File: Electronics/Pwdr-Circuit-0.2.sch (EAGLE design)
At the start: 23 parts, among them U1 LM317T, U2 ARDUINO-MEGASHIELD, U5 ULN2003, U6 ULN2003

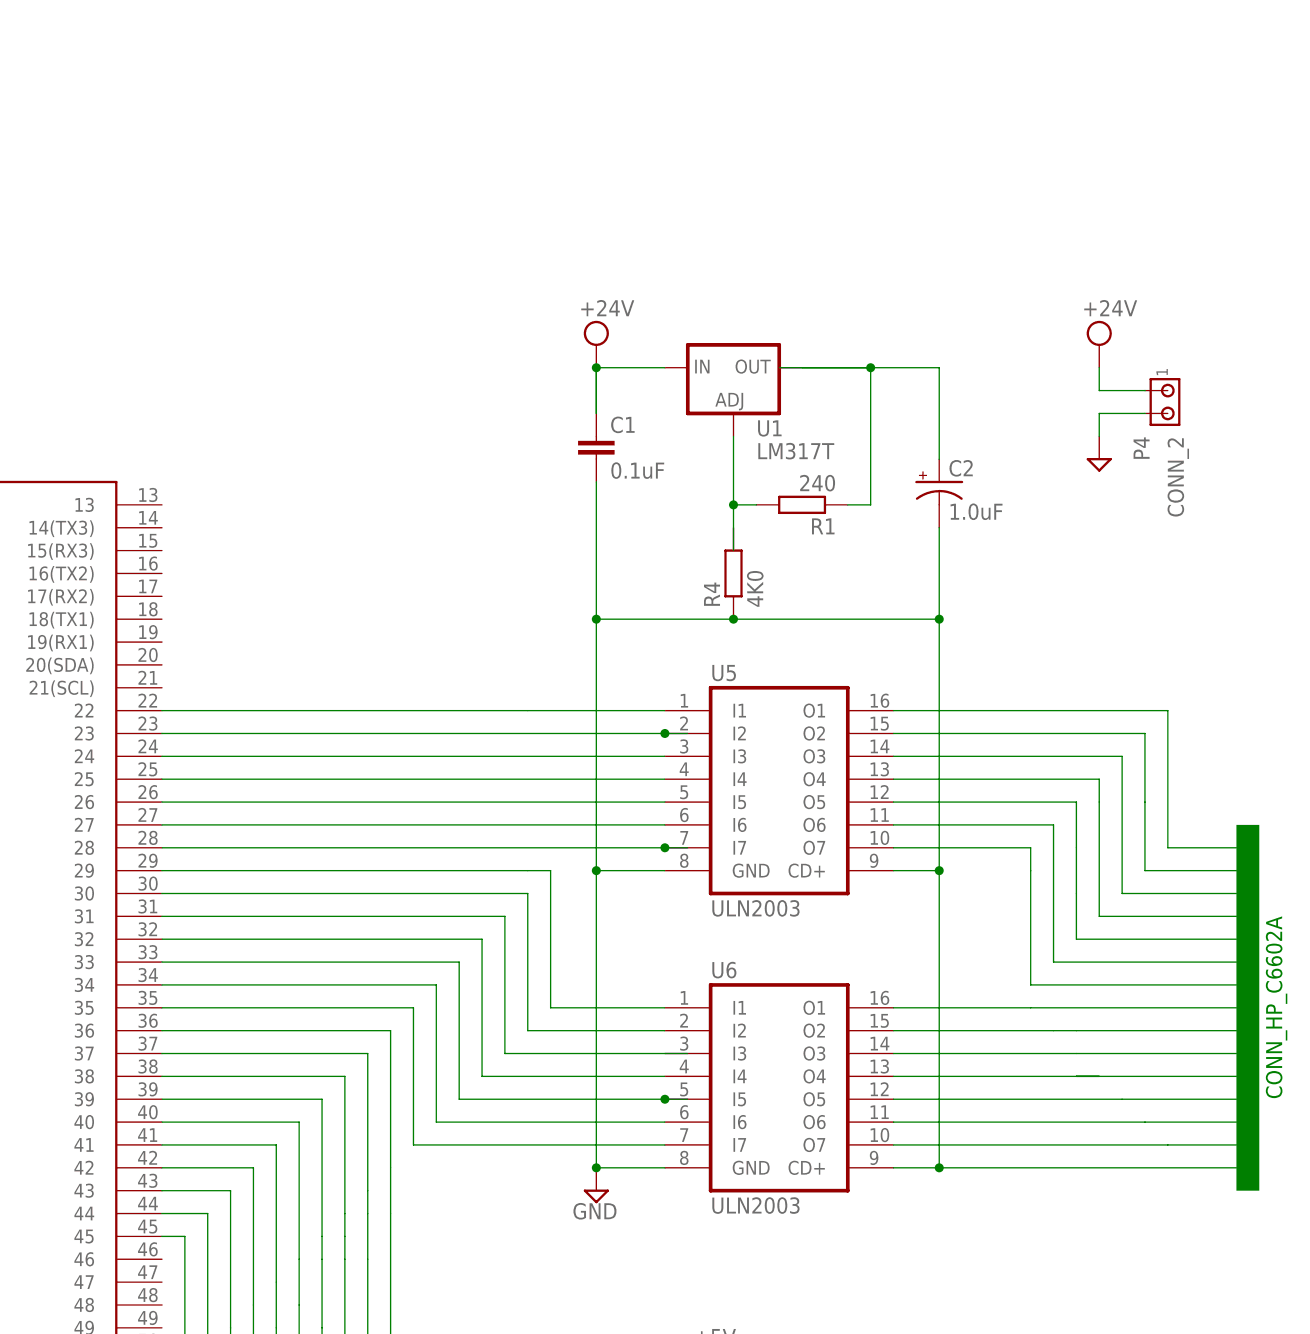
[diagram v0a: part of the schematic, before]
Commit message: Added shutdown to schematic.
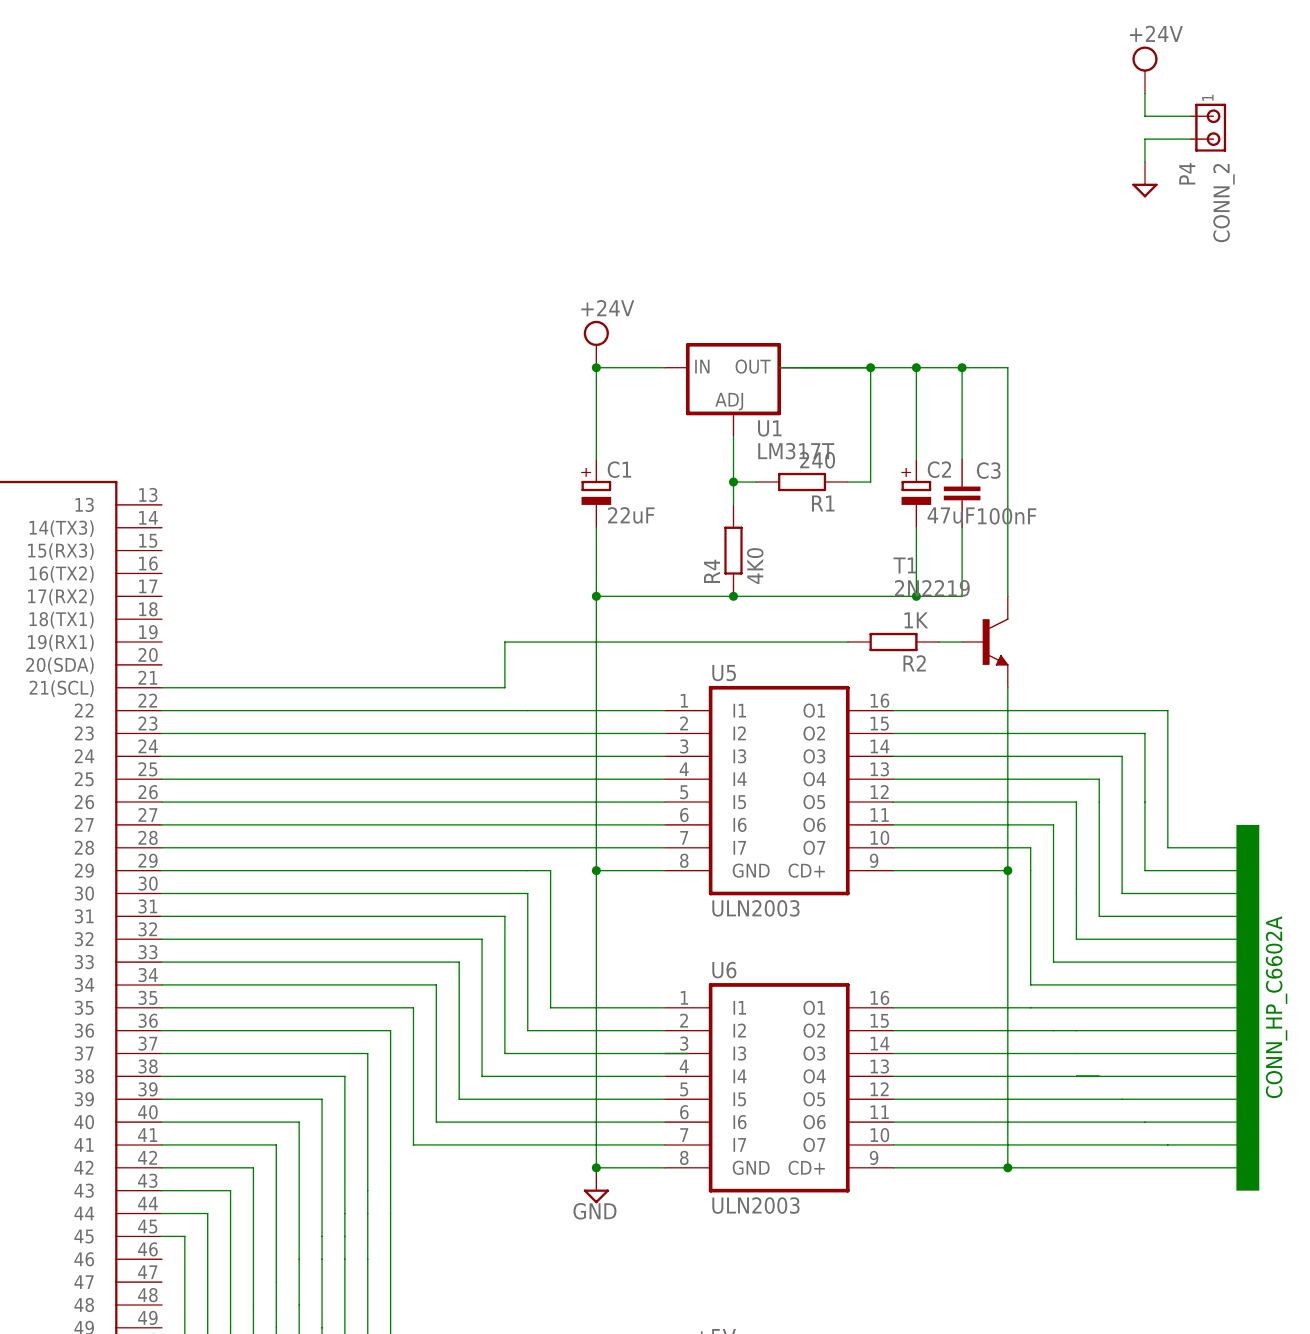
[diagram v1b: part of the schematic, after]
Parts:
- added C3: 100nF, resistor:C-EU025-024X044
- added R2: 1K, rcl:R-EU_0204/2V
- added T1: 2N2219, transistor:2N2219
- C1: value 0.1uF -> 22uF; device rcl:C-EU025-024X044 -> rcl:CPOL-EUE2.5-6
- C2: value 1.0uF -> 47uF; device rcl:CPOL-US085CS-1AR -> rcl:CPOL-EUE2.5-6
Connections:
- new net N$29: T1.E, U5.CD+, U6.CD+
- new net N$67: R2.2, U2.21(SCL)
- new net N$68: R2.1, T1.B
- net AGND: now also C1.-, C3.2; no longer C1.2, U5.CD+, U6.CD+
- net N$2: now also C3.1, T1.C
- net VCC: now also C1.+; no longer C1.1
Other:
- moved on the sheet: C2, CONN_2, R1, R4
